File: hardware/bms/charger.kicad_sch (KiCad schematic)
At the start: 1 part

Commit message: More charger sch progress
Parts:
- added C2: 10uF, symbol Device:C_Small
- added C? (x3): 0.1uF, Capacitor_SMD:C_0603_1608Metric, symbol Device:C_Small
- added C?: 1uF, Capacitor_SMD:C_0805_2012Metric, symbol Device:C_Small
- added C?: 1uF, Capacitor_SMD:C_0603_1608Metric, symbol Device:C_Small
- added C?: 56nF, Capacitor_SMD:C_0603_1608Metric, symbol Device:C_Small
- added D?: BLUE, symbol Device:LED_Small
- added L1: 3.3uH, symbol Device:L
- added Q?: Q_NMOS_SGD, bms:PG-TDSON-8, symbol Device:Q_NMOS_SGD
- added R?: 10k, Resistor_SMD:R_0603_1608Metric, symbol Device:R_Small_US
- added R?: 44.2k, Resistor_SMD:R_0603_1608Metric, symbol Device:R_Small_US
- added R? (x2): 100k, Resistor_SMD:R_0603_1608Metric, symbol Device:R_Small_US
- added R?: 137k, Resistor_SMD:R_0603_1608Metric, symbol Device:R_Small_US
- added R?: ~, Resistor_SMD:R_0603_1608Metric, symbol Device:R_Small_US
- added R?: 10R, Resistor_SMD:R_0603_1608Metric, symbol Device:R_Small_US
- added U?: LM74700, Package_TO_SOT_SMD:SOT-23-6, symbol Power_Management:LM74700
- U?: footprint (none) -> Package_DFN_QFN:VQFN-24-1EP_4x4mm_P0.5mm_EP2.45x2.45mm; MFG (none) -> Texas Instruments; MFG PN (none) -> BQ24610RGER
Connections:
- net CHG_IN+: now also C?.2, C?.2, Q?.1 (S), R?.1, U?.6 (ANODE)
- net CHG_IN_PROT: now reaches U?.1 (ACN)
- net CHG_IN_PROT: now also U?.2 (ACP), C?.2, Q?.3 (D), R?.1, U?.4 (CATHODE)
- net VREF: now reaches U?.10 (VREF)
- net VREF: now also U?.16 (ACSET), U?.4 (CE), C?.1, R?.2, R?.2, R?.2
- net ISET1: now reaches U?.11 (ISET1)
- net ISET1: now also R?.1, R?.2
- net ISET2: now reaches U?.15 (ISET2)
- net ISET2: now also R?.1, R?.2
- net GND: now reaches U?.17 (GND)
- net GND: now also U?.25 (GND), C?.1, C?.1, C?.2, C?.2, C?.2, R?.1, R?.1, U?.2 (GND)
- net C_VCC: now reaches U?.24 (VCC)
- net C_VCC: now also C?.1, R?.2
- net STAT1: now reaches U?.5 (STAT1)
- net STAT1: now also D?.1 (K)
- net TS: now reaches U?.6 (TS)
- net TTC: now reaches U?.7 (TTC)
- net TTC: now also C?.1
- net ~{PG}: now reaches U?.8 (~{PG})
- net STAT2: now reaches U?.9 (STAT2)
- new net: Q?.2 (G), U?.5 (GATE)
- new net: C?.1, U?.1 (VCAP)
- new net: R?.2, U?.3 (EN)
- new net: D?.2 (A), R?.1
- no-connect marks 0 -> 2
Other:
- note added: "ACSET not used, tied to VREF"
- note added: "Battery monitor will cut off charge voltage path."
- note added: "CHARGE CURRENT SETTINGS"
- note added: "I_CHG = 5 * VSET1 I_CHG = 9.5A"
- note added: "I_CHG_TERM = 1 * VSET2 I_CHG_TERM = 100mA * 10P = 1A"
- note added: "Ideal diode controller enabled by default, acts as a diode to block reverse current."
- note added: "Mark Belbin"
- note added: "NMOS blocks reverse voltage on charger input, acts as a diode"
- note added: "STATUS LEDS"
- note added: "TCHARGE_MAX = 5.6 min/nF 56 * 5.6 ~= 5.2h"
- note added: "VREF = 3V3"
- note added: "eSUP BMS - Charger"
- moved on the sheet: U?

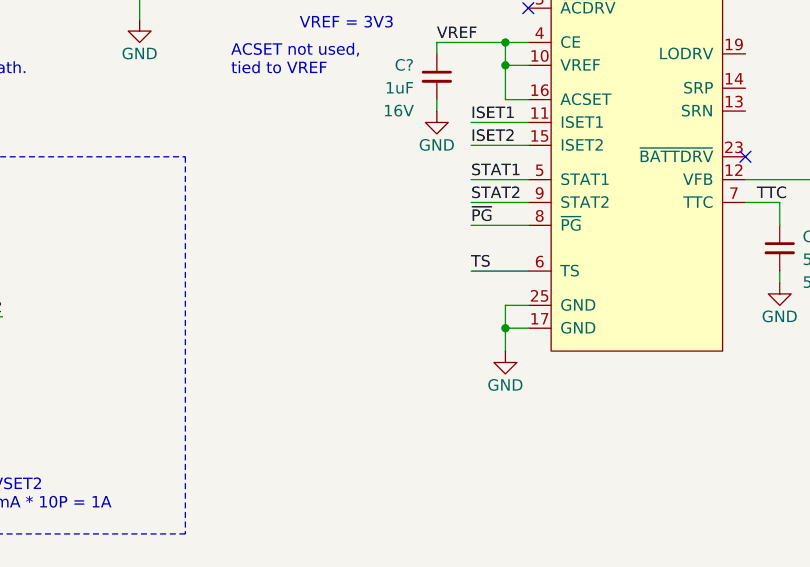
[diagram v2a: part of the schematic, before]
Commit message: Added another thermistor for charger temp sensings. 9 total for the whole pack now
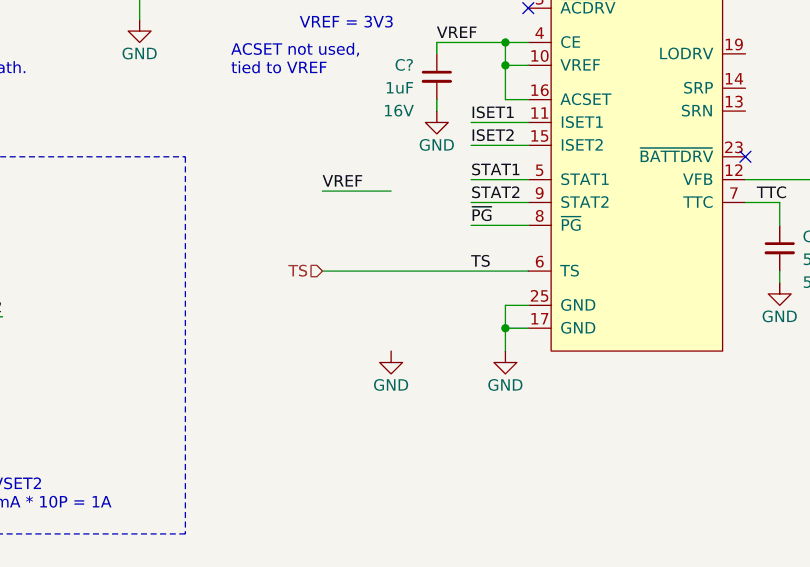
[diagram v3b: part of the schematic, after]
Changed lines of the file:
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@@
     (stroke (width 0) (type default))
   )
-  (wire (pts (xy 135.89 106.68) (xy 142.24 106.68))
+  (wire (pts (xy 119.38 106.68) (xy 142.24 106.68))
     (stroke (width 0) (type default))
   )
@@
   )
   (wire (pts (xy 71.12 46.99) (xy 80.01 46.99))
+    (stroke (width 0) (type default))
+  )
+  (wire (pts (xy 119.38 97.79) (xy 127 97.79))
     (stroke (width 0) (type default))
   )
@@
     (effects (font (size 1.27 1.27)) (justify right bottom))
   )
+  (label "VREF" (at 119.38 97.79 0) (fields_autoplaced)
+    (effects (font (size 1.27 1.27)) (justify left bottom))
+  )
   (hierarchical_label "CHG_IN+" (shape input) (at 31.75 46.99 180) (fields_autoplaced)
     (effects (font (size 1.27 1.27)) (justify right))
@@
   (hierarchical_label "CHG_OUT+" (shape output) (at 247.65 78.74 0) (fields_autoplaced)
     (effects (font (size 1.27 1.27)) (justify left))
+  )
+  (hierarchical_label "TS" (shape input) (at 119.38 106.68 180) (fields_autoplaced)
+    (effects (font (size 1.27 1.27)) (justify right))
   )
   (symbol (lib_id "bms:BQ24610") (at 170.18 59.69 0) (unit 1)
@@
         )
       )
+    )
+  )
+  (symbol (lib_id "power:GND") (at 127 115.57 0) (unit 1)
+    (in_bom yes) (on_board yes) (dnp no)
+    (property "Reference" "#PWR012" (at 127 121.92 0)
+      (effects (font (size 1.27 1.27)) hide)
+    )
+    (property "Value" "GND" (at 127 119.38 0)
+      (effects (font (size 1.27 1.27)))
+    )
+    (property "Footprint" "" (at 127 115.57 0)
+      (effects (font (size 1.27 1.27)) hide)
+    )
+    (property "Datasheet" "" (at 127 115.57 0)
+      (effects (font (size 1.27 1.27)) hide)
+    )
+    (pin "1")
+    (instances
+      (project "bms"
+        (path "/a4805e9d-b940-444e-a7cb-db4f4c53ed46/00000000-0000-0000-0000-00006523ab32"
+          (reference "#PWR012") (unit 1)
+        )
+      )

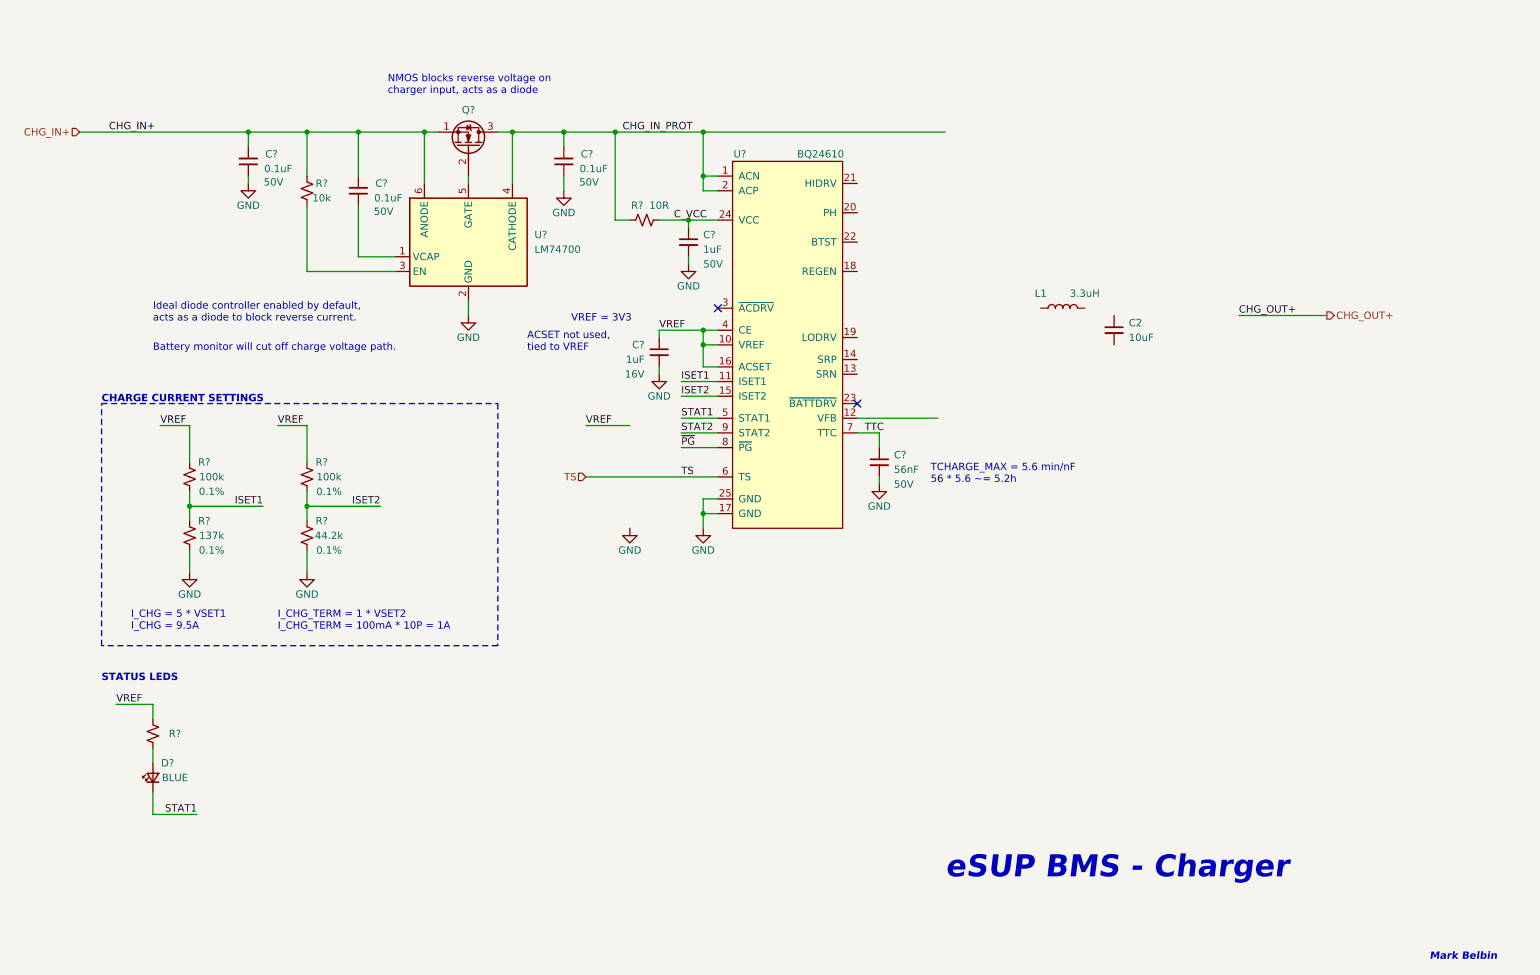
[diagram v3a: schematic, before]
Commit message: Made more progress on charger sch. Need to complete power stage next. Also added diode OR for MCU power conv input. Still deciding on converter selection
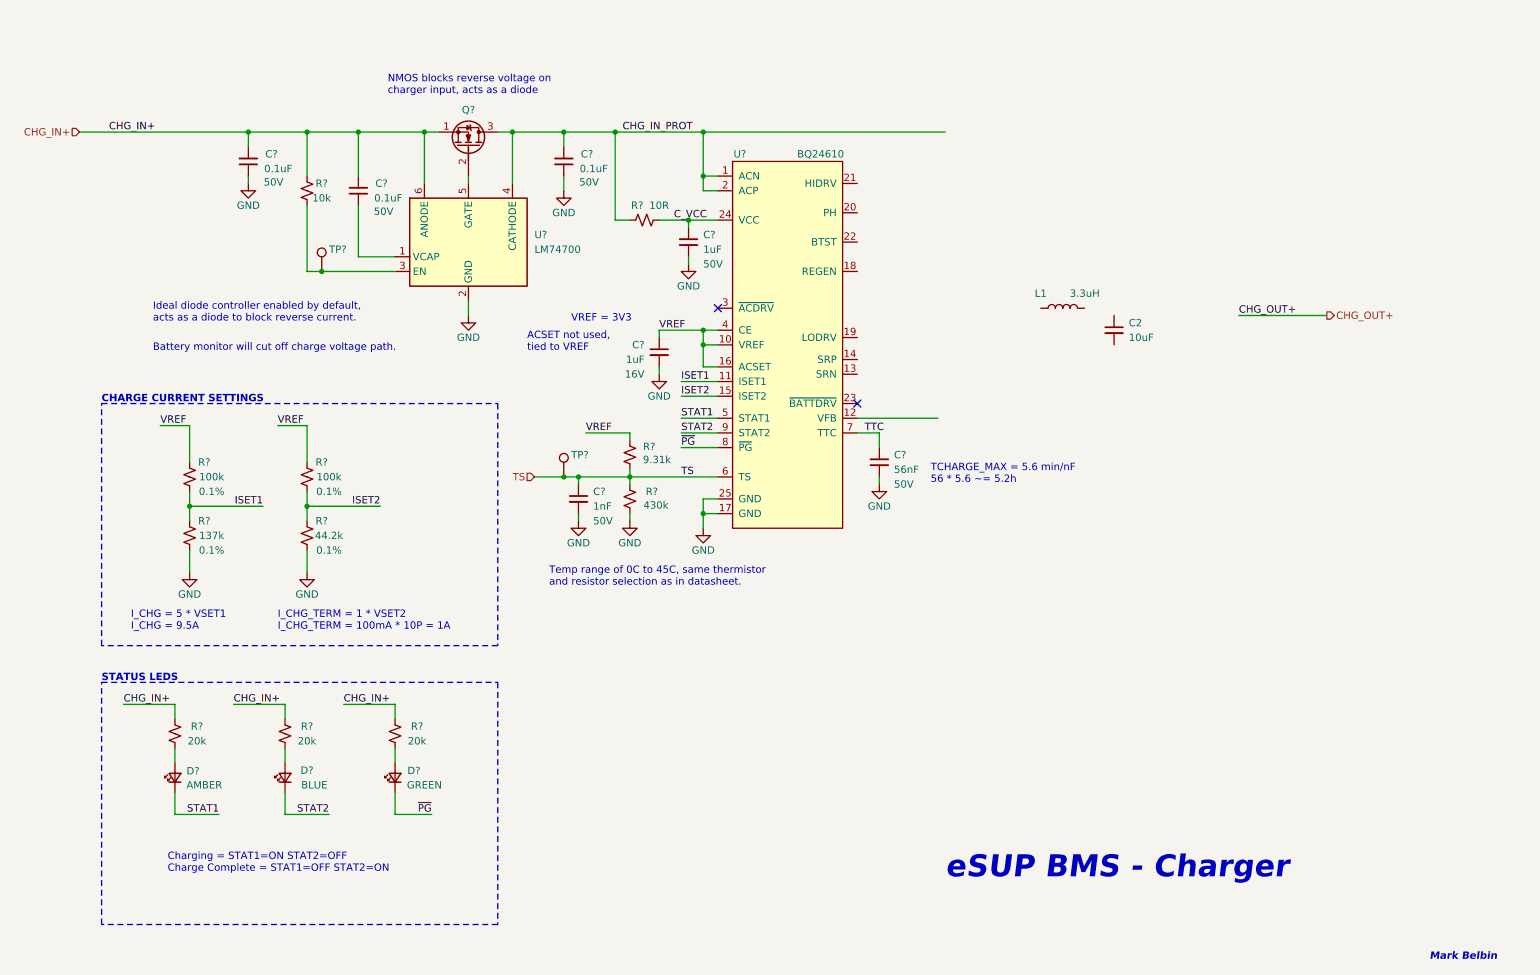
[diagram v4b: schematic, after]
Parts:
- added C?: 1nF, Capacitor_SMD:C_0603_1608Metric, symbol Device:C_Small
- added D?: AMBER, LED_SMD:LED_0603_1608Metric, symbol Device:LED_Small
- added D?: GREEN, LED_SMD:LED_0603_1608Metric, symbol Device:LED_Small
- added R? (x2): 20k, Resistor_SMD:R_0603_1608Metric, symbol Device:R_Small_US
- added R?: 430k, Resistor_SMD:R_0603_1608Metric, symbol Device:R_Small_US
- added R?: 9.31k, Resistor_SMD:R_0603_1608Metric, symbol Device:R_Small_US
- added TP? (x2): TestPoint, TestPoint:TestPoint_Pad_D1.0mm, symbol Connector:TestPoint
- D?: footprint (none) -> LED_SMD:LED_0603_1608Metric; MFG (none) -> Würth Elektronik; MFG PN (none) -> 150060BS75000; VF (none) -> 3.2V
- R?: value ~ -> 20k; MFG PN (none) -> ERJ-3EKF2002V
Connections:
- net CHG_IN+: now also R?.2, R?.2, R?.2
- net GND: now also C?.2, R?.1
- net STAT1: now also D?.1 (K); no longer D?.1 (K)
- net STAT2: now also D?.1 (K)
- net TS: now also C?.1, R?.1, R?.2, TP?.1
- net VREF: now also R?.2; no longer R?.2
- net ~{PG}: now also D?.1 (K)
- net at R?.2, U?.3 (EN): now also TP?.1
- new net: D?.2 (A), R?.1 (x2)
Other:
- note added: "Charging = STAT1=ON STAT2=OFF Charge Complete = STAT1=OFF STAT2=ON"
- note added: "Temp range of 0C to 45C, same thermistor and resistor selection as in datasheet."
- moved on the sheet: D?, R?

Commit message: Selected charger FETs, replaced other charger FETs to match. FETs rated for 40V since this is a 6S board (25.2V MAX). Also downsized the discharge FETs to be smaller and cheaper by selecting 40V FETs.
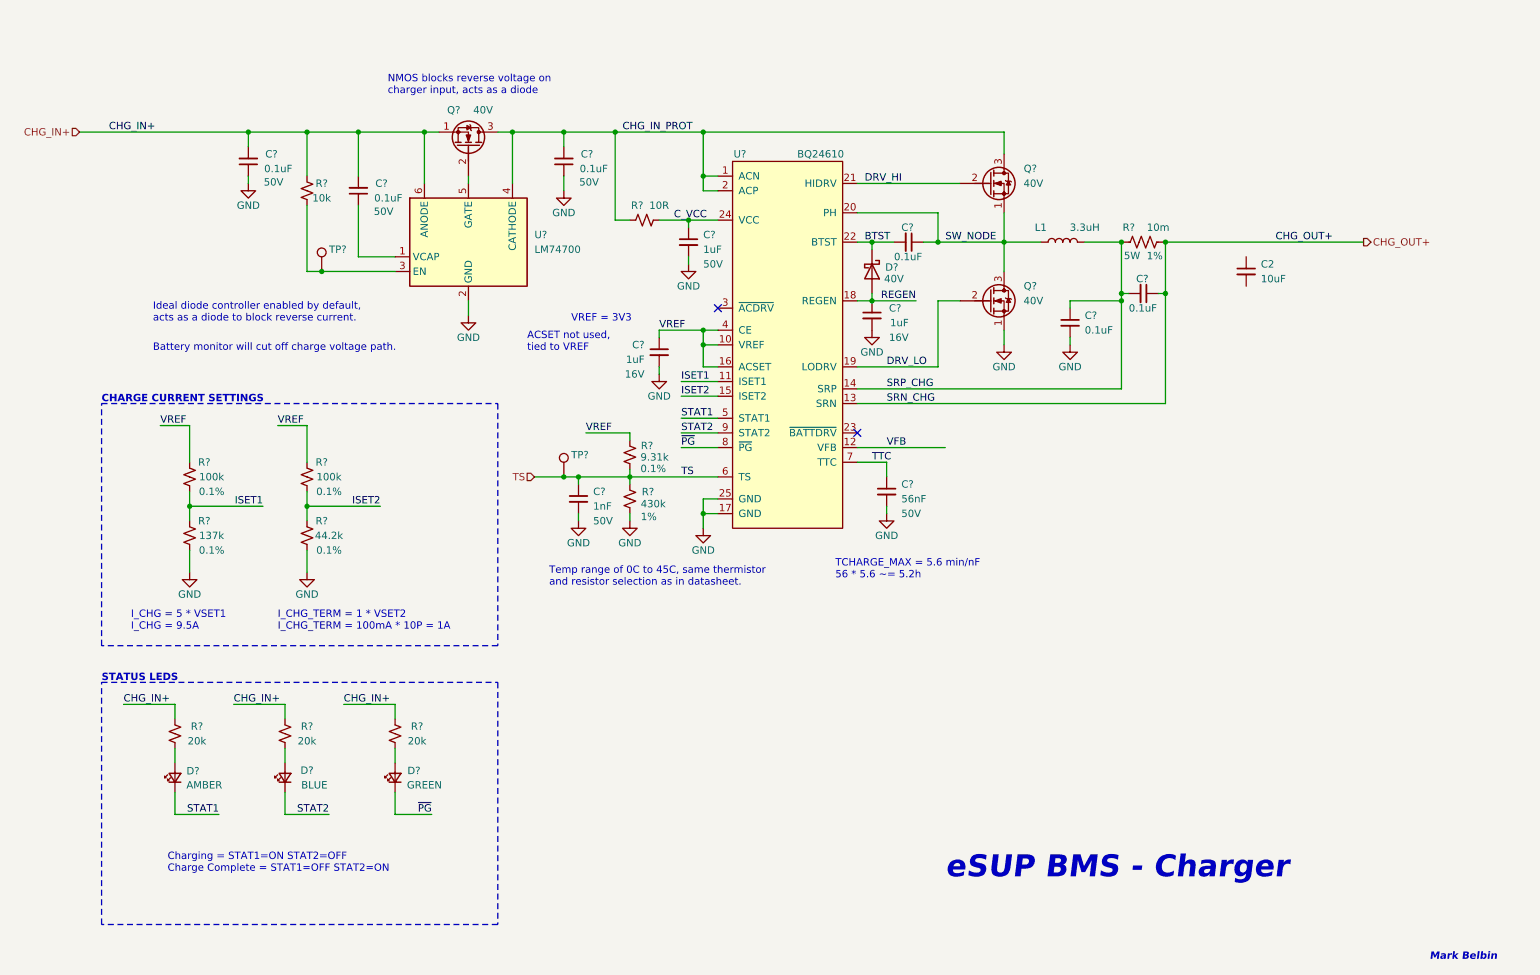
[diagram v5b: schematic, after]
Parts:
- removed Q?: Q_NMOS_SGD, bms:PG-TDSON-8, symbol Device:Q_NMOS_SGD
- added C? (x3): 0.1uF, Capacitor_SMD:C_0603_1608Metric, symbol Device:C_Small
- added C?: 1uF, Capacitor_SMD:C_0603_1608Metric, symbol Device:C_Small
- added D?: D_Schottky, Diode_SMD:D_SOD-523, symbol Device:D_Schottky
- added Q? (x3): BSZ018N04LS6ATMA1, bms:PG-TSDSON-8-26_INF, symbol Device:Q_NMOS_SGD
- added R?: 10m, Resistor_SMD:R_2512_6332Metric, symbol Device:R_US
- R?: Tolerance (none) -> 1%
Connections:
- net CHG_IN+: now also Q?.1 (S)
- net CHG_IN_PROT: now also Q?.3 (D), Q?.3 (D)
- net CHG_OUT+: now also U?.13 (SRN), C?.1, R?.1
- net GND: now also C?.2, C?.2, Q?.1 (S)
- net VFB: now reaches U?.12 (VFB)
- net SRP_CHG: now reaches U?.14 (SRP)
- net SRP_CHG: now also L1.2, C?.1, C?.2, R?.2
- net REGEN: now reaches U?.18 (REGEN)
- net REGEN: now also C?.1, D?.2 (A)
- net DRV_LO: now reaches U?.19 (LODRV)
- net DRV_LO: now also Q?.2 (G)
- net SW_NODE: now reaches U?.20 (PH)
- net SW_NODE: now also L1.1, C?.1, Q?.1 (S), Q?.3 (D)
- net DRV_HI: now reaches U?.21 (HIDRV)
- net DRV_HI: now also Q?.2 (G)
- net BTST: now reaches U?.22 (BTST)
- net BTST: now also C?.2, D?.1 (K)
- net at U?.5 (GATE): now also Q?.2 (G)
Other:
- moved on the sheet: C2, C?, L1
